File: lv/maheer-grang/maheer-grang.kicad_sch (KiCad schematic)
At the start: 0 parts

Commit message: final draft for pe onboarding
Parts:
- added C1, C4, C5, C6, C7, C8, C9: C_Small, symbol Device:C_Small
- added J1: Conn_01x05, symbol Connector_Generic:Conn_01x05
- added J3: Conn_01x09, symbol Connector_Generic:Conn_01x09
- added R1: R_Small_US, symbol Device:R_Small_US
- added U1: TLV320AIC3100, Package_DFN_QFN:VQFN-32-1EP_5x5mm_P0.5mm_EP3.5x3.5mm, symbol Audio:TLV320AIC3100
- added U3: AP2112K-3.3, Package_TO_SOT_SMD:SOT-23-5, symbol Regulator_Linear:AP2112K-3.3
- added U4: AP2112K-1.8, Package_TO_SOT_SMD:SOT-23-5, symbol Regulator_Linear:AP2112K-1.8
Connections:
- new net: C4.1, U1.17 (AVDD)
- new net: C4.2, C6.2, C7.2, U3.5 (VOUT), U4.1 (VIN), U4.3 (EN)
- new net: C1.1, U1.14 (MIC1RP)
- new net: C6.1, U1.28 (HPVDD)
- new net: C9.1, U1.24 (SPKVDD)
- new net: R1.1, U1.12 (MICBIAS)
- new net: C5.2, U4.5 (VOUT)
- new net: J3.5 (Pin_5), U1.10 (SCL)
- new net: C7.1, U1.2 (IOVDD)
- new net: C8.1, U1.21 (SPKVDD)
- new net: C5.1, U1.3 (DVDD)
- new net: J3.8 (Pin_8), U1.31 (~{RESET})
- new net: J3.3 (Pin_3), U1.4 (DOUT)
- new net: J3.4 (Pin_4), U1.5 (DIN)
- new net: J3.2 (Pin_2), U1.6 (WCLK)
- new net: J3.1 (Pin_1), U1.7 (BCLK)
- new net: J3.7 (Pin_7), U1.8 (MCLK)
- new net: J3.6 (Pin_6), U1.9 (SDA)
- new net +5V: C8.2, C9.2, U3.1 (VIN), U3.3 (EN)
- new net GNDREF: J1.3 (Pin_3), J1.5 (Pin_5), J3.9 (Pin_9), U1.1 (IOVSS), U1.16 (AVSS), U1.18 (DVSS), U1.20 (SPKVSS), U1.25 (SPKVSS), U1.29 (HPVSS), U1.33 (EP), U3.2 (GND), U4.2 (GND)
- new net MIC: C1.2, J1.4 (Pin_4), R1.2
- new net SPK1: J1.1 (Pin_1), U1.22 (SPKP), U1.26 (SPKP)
- new net SPK2: J1.2 (Pin_2), U1.19 (SPKM), U1.23 (SPKM)

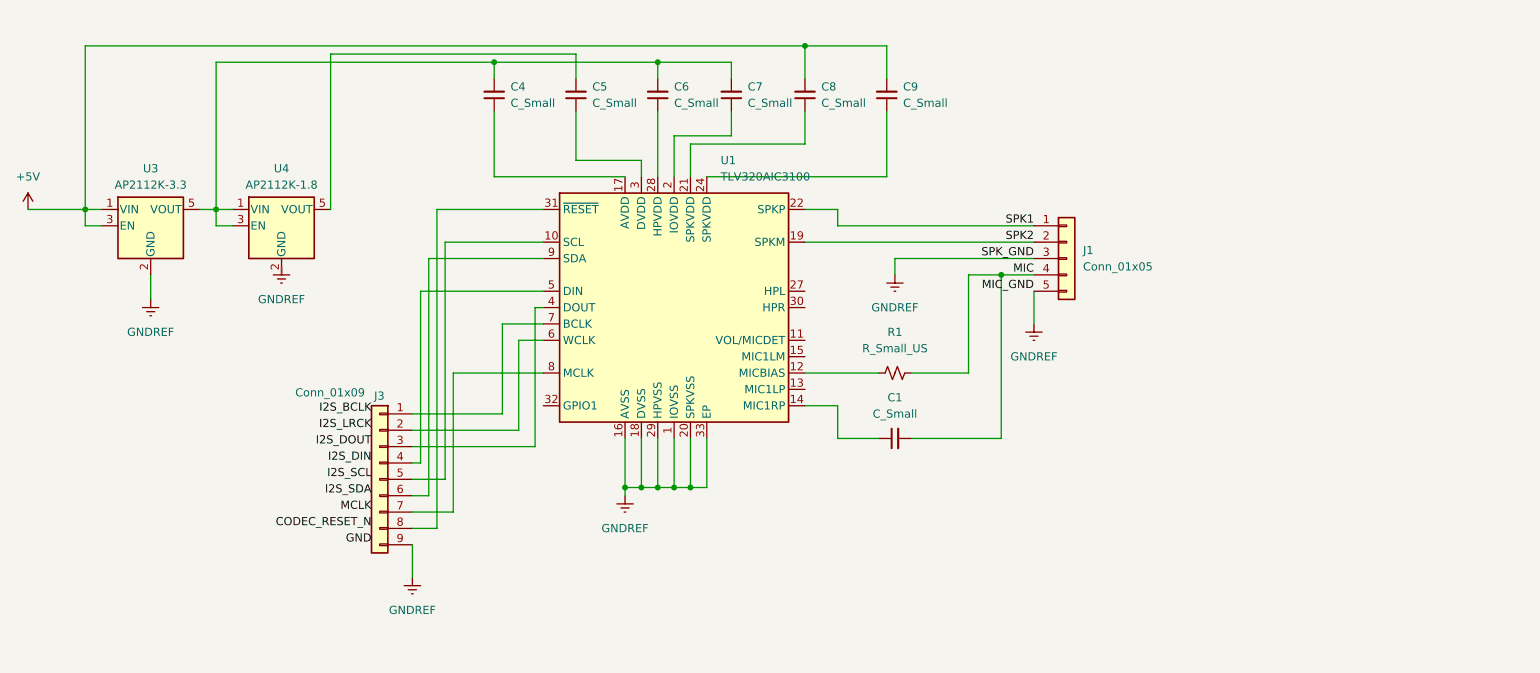
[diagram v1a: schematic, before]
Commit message: lv final draft: files for submission are the excel spreadsheet, the writeup, and the kicad schematic for the driver audio project
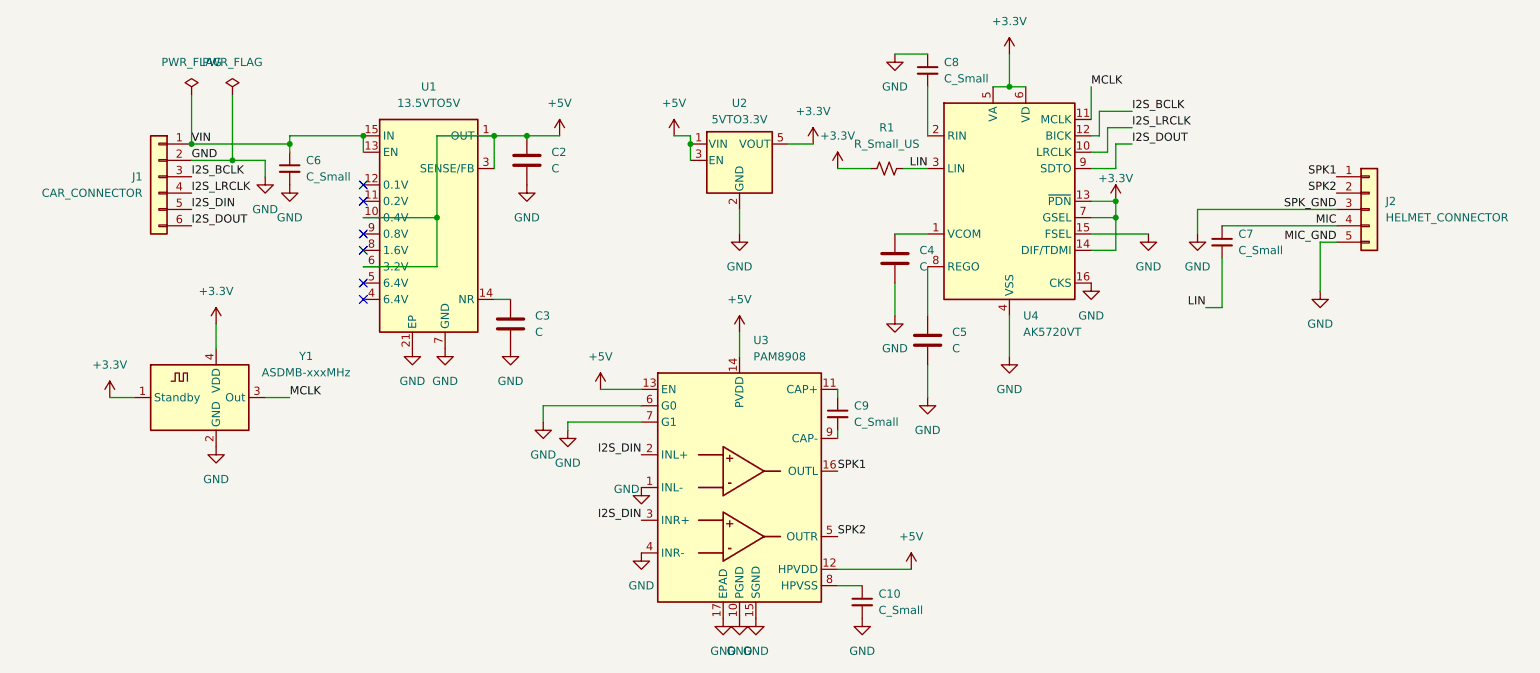
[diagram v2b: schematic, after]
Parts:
- removed C1, C4, C5: C_Small, symbol Device:C_Small
- removed J1: Conn_01x05, symbol Connector_Generic:Conn_01x05
- removed J3: Conn_01x09, symbol Connector_Generic:Conn_01x09
- removed U1: TLV320AIC3100, Package_DFN_QFN:VQFN-32-1EP_5x5mm_P0.5mm_EP3.5x3.5mm, symbol Audio:TLV320AIC3100
- removed U3: AP2112K-3.3, Package_TO_SOT_SMD:SOT-23-5, symbol Regulator_Linear:AP2112K-3.3
- removed U4: AP2112K-1.8, Package_TO_SOT_SMD:SOT-23-5, symbol Regulator_Linear:AP2112K-1.8
- added C10: C_Small, symbol Device:C_Small
- added C2, C3, C4, C5: C, symbol Device:C
- added J1: CAR_CONNECTOR, symbol Connector_Generic:Conn_01x06
- added J2: HELMET_CONNECTOR, symbol Connector_Generic:Conn_01x05
- added U1: 13.5VTO5V, Package_DFN_QFN:Texas_RGW0020A_VQFN-20-1EP_5x5mm_P0.65mm_EP3.15x3.15mm_ThermalVias, symbol Regulator_Linear:TPS7A4701xRGW
- added U2: 5VTO3.3V, Package_TO_SOT_SMD:SOT-23-5, symbol Regulator_Linear:AP2112K-3.3
- added U3: PAM8908, Package_DFN_QFN:QFN-16-1EP_3x3mm_P0.5mm_EP1.7x1.7mm, symbol Amplifier_Audio:PAM8908
- added U4: AK5720VT, Package_SO:TSSOP-16_4.4x5mm_P0.65mm, symbol Audio:AK5720VT
- added Y1: ASDMB-xxxMHz, Oscillator:Oscillator_SMD_Abracon_ASDMB-4Pin_2.5x2.0mm, symbol Oscillator:ASDMB-xxxMHz
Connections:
- net +5V: now also C2.1, U1.1 (OUT), U1.10 (0.4V), U1.20 (OUT), U1.3 (SENSE/FB), U1.6 (3.2V), U2.1 (VIN), U2.3 (EN), U3.12 (HPVDD), U3.13 (EN), U3.14 (PVDD); no longer C8.2, C9.2
- net GND: now also C6.2, C8.1, C10.2, C2.2, C3.2, C4.2, C5.2, J1.2 (Pin_2), J2.3 (Pin_3), J2.5 (Pin_5), U1.21 (EP), U1.7 (GND), U2.2 (GND), U3.1 (INL-), U3.10 (PGND), U3.15 (SGND), U3.17 (EPAD), U3.4 (INR-), U3.6 (G0), U3.7 (G1), U4.15 (FSEL), U4.16 (CKS), U4.4 (VSS), Y1.2 (GND)
- net I2S_BCLK: now also J1.3 (Pin_3), U4.12 (BICK)
- net I2S_DIN: now also J1.5 (Pin_5), U3.2 (INL+), U3.3 (INR+)
- net I2S_DOUT: now also J1.6 (Pin_6), U4.9 (SDTO)
- net MCLK: now also U4.11 (MCLK), Y1.3 (Out)
- net MIC: now also C7.1, J2.4 (Pin_4); no longer R1.2
- net SPK1: now also J2.1 (Pin_1), U3.16 (OUTL)
- net SPK2: now also J2.2 (Pin_2), U3.5 (OUTR)
- net LIN: now reaches C7.2
- net LIN: now also R1.2, U4.3 (LIN); no longer C6.2
- net VIN: now reaches C6.1
- net VIN: now also J1.1 (Pin_1), U1.13 (EN), U1.15 (IN), U1.16 (IN)
- net at C9.1: now also U3.11 (CAP+)
- net +3.3V: now reaches R1.1
- net +3.3V: now also U2.5 (VOUT), U4.13 (~{PDN}), U4.14 (DIF/TDMI), U4.5 (VA), U4.6 (VD), U4.7 (GSEL), Y1.1 (Standby), Y1.4 (VDD)
- new net: C4.1, U4.1 (VCOM)
- new net: C8.2, U4.2 (RIN)
- new net: C5.1, U4.8 (REGO)
- new net: C3.1, U1.14 (NR)
- new net: C10.1, U3.8 (HPVSS)
- new net: C9.2, U3.9 (CAP-)
- new net I2S_LRCLK: J1.4 (Pin_4), U4.10 (LRCLK)
- no-connect marks 0 -> 6
